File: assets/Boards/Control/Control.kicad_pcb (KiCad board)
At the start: 2 copper layers, 59.7 x 22.9 mm, 13 parts, among them J3 MAIN_BOARD, J5 MIC, SW1 SW_Push_Dual, U1 TLV70033_SOT23-5

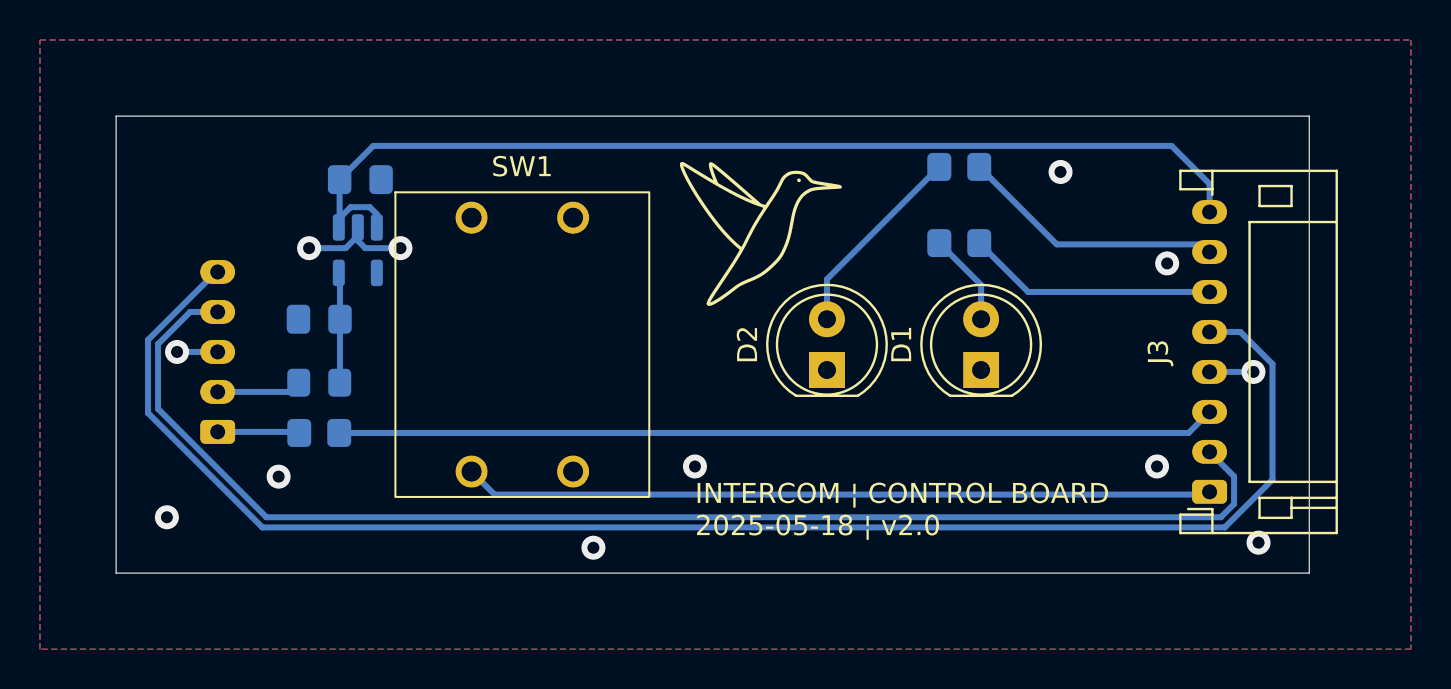
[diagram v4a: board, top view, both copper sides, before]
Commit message: Applied suggestions from people from the KiCad forum.
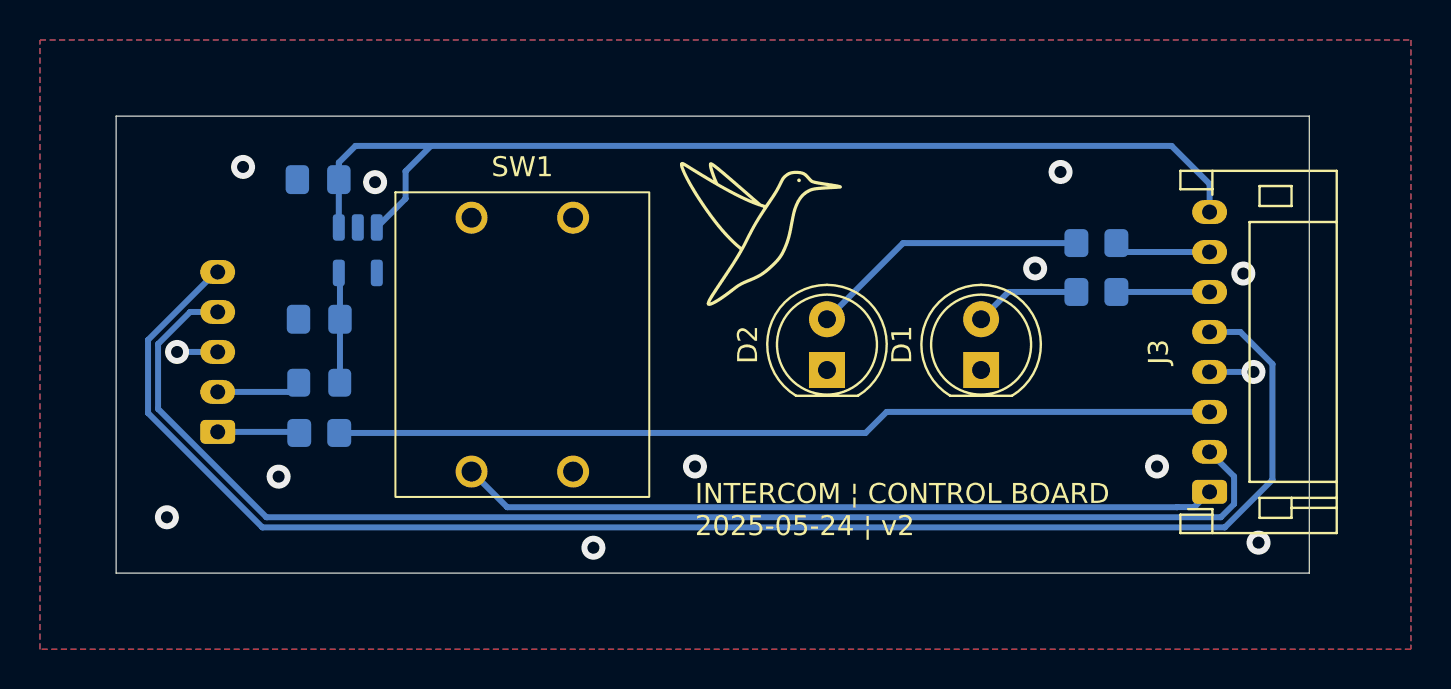
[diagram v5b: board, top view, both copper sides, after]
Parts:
- moved R2 7.85 mm to (169.7, 99.1)
- moved R1 7.28 mm to (169.7, 101.5)
- moved C1 2.11 mm to (130.8, 95.9), turned to 0 degrees
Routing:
- net LG: track 13.3 -> 4.85 mm
- net LR: track 12.5 -> 4.66 mm
- net GND: track 10.3 -> 4.23 mm, vias 12 -> 13
- net Net-(D2-A): track 9.95 -> 14.1 mm
- net +5V: track 52.2 -> 54.5 mm
- net PB: track 37.5 -> 38.2 mm
- net Net-(D1-A): track 4.68 -> 5.33 mm
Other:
- board text added: "INTERCOM ¦ CONTROL BOARD 2025-05-24 ¦ v2"
- board text removed: "INTERCOM ¦ CONTROL BOARD 2025-05-18 ¦ v2.0"

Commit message: Updated boards.
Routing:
- net +5V: track 54.5 -> 53.1 mm
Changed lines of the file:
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@@
+	)
+	(segment
+		(start 133.6904 96.8604)
+		(end 133.6904 98.2781)
+		(width 0.3)
+		(layer "B.Cu")
+		(net 3)
 	)
 	(segment
@@
 	)
 	(segment
-		(start 135.128 96.8405)
-		(end 135.128 95.469)
+		(start 132.7156 95.8856)
+		(end 133.6904 96.8604)
+		(width 0.3)
+		(layer "B.Cu")
+		(net 3)
+	)
+	(segment
+		(start 131.7904 95.8856)
+		(end 132.7156 95.8856)
 		(width 0.3)
 		(layer "B.Cu")
@@
 		(start 175.35 96.102)
 		(end 173.447 94.199)
-		(width 0.3)
-		(layer "B.Cu")
-		(net 3)
-	)
-	(segment
-		(start 135.128 95.469)
-		(end 136.398 94.199)
 		(width 0.3)
 		(layer "B.Cu")
@@
 		(start 173.447 94.199)
 		(end 136.398 94.199)
-		(width 0.3)
-		(layer "B.Cu")
-		(net 3)
-	)
-	(segment
-		(start 133.6904 98.2781)
-		(end 135.128 96.8405)
 		(width 0.3)
 		(layer "B.Cu")
@@
 	)
 	(via
-		(at 133.604 96.012)
+		(at 135.128 95.504)
 		(size 1.2)
 		(drill 0.6)
